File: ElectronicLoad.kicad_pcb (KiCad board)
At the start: 4 copper layers, 100 x 65 mm, 93 parts, among them J1 USB_B, J2 TagConnect, J3 ICSP, J4 Load, Q1 MTP3055VL, Q2 DMG2302U, SW1 RESET, SW2 BOOTLOADER, SW3 Control, U1 TLC272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

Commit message: Move connectors
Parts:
- moved LCD1 86.4 mm to (119.9, 102.1)
- moved C23 74.5 mm to (122.9, 94.5)
- moved C19 74.5 mm to (120.9, 94.5)
- moved C21 74.5 mm to (118.9, 94.5)
- moved RN2 74.5 mm to (120.6, 89.9)
- moved SW3 74.5 mm to (112.8, 85.3)
- moved C11 73.5 mm to (190.5, 95.0)
- moved C14 73.5 mm to (160.8, 87.9)
- moved C17 73.5 mm to (140.7, 112.0)
- moved C5 73.5 mm to (140.7, 116.6)
- moved C6 73.5 mm to (140.7, 114.3)
- moved H2 73.5 mm to (200.4, 71.7)
- moved H3 73.5 mm to (200.4, 126.7)
- moved Q1 73.5 mm to (196.6, 96.5)
- moved RN3 73.5 mm to (155.4, 114.3)
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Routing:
- net ROT_SW: track 68.0 -> 56.7 mm
- net Net-(RN1-Pad3): track 65.7 -> 55.6 mm
- net SCL: track 128.8 -> 137.0 mm
- net SDA: track 127.3 -> 134.8 mm, vias 5 -> 6
- net VLOAD: track 133.5 -> 138.9 mm
- net /D_USB-: track 20.1 -> 22.9 mm
- net /D_USB+: track 25.5 -> 28.2 mm
- net ROT_A: track 35.2 -> 36.3 mm
- net VREF2048: track 28.4 -> 27.3 mm
- net /ILOAD+: track 101.1 -> 102.1 mm
- net FAN_PWM: track 62.9 -> 62.2 mm
- net VCC: track 121.5 -> 120.9 mm
- net /XTAL2: track 17.8 -> 18.4 mm

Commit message: Cleanup
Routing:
- net ~RXLED: track 66.5 -> 36.7 mm, vias 2 -> 0
- net ~TXLED: track 46.3 -> 39.2 mm
- net SDA: track 134.8 -> 137.5 mm, vias 6 -> 5
- net Net-(RN1-Pad3): track 55.6 -> 53.7 mm
- net ROT_SW: track 56.7 -> 55.2 mm
- net SCL: track 137.0 -> 135.5 mm
- net Net-(LED3-Pad2): track 23.3 -> 21.9 mm
- net Net-(LED2-Pad2): track 24.9 -> 23.6 mm
- net /Vin-: track 11.6 -> 12.7 mm
- net Net-(LED1-Pad2): track 26.5 -> 25.5 mm
- net /XTAL2: track 18.4 -> 18.9 mm

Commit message: Cleanup
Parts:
- moved RN3 16.3 mm to (143.8, 125.7), turned to 90 degrees
- moved C2 1.61 mm to (158.0, 97.0), turned to 180 degrees
- moved C4 1.61 mm to (158.0, 99.6), turned to 180 degrees
- moved U5 1.44 mm to (158.0, 93.5), turned to 90 degrees
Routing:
- net FAN_PWM: track 62.2 -> 39.9 mm
- net Net-(LED3-Pad2): track 21.9 -> 6.94 mm
- net Net-(LED2-Pad2): track 23.6 -> 10.7 mm
- net Net-(LED1-Pad2): track 25.5 -> 15.6 mm
- net /ISET: track 19.5 -> 14.5 mm
- net SCL: track 135.5 -> 139.5 mm, vias 4 -> 5
- net Net-(RN1-Pad3): track 53.7 -> 50.3 mm
- net SDA: track 137.5 -> 140.6 mm, vias 5 -> 6
- net ~OT_SHUTDOWN: track 61.3 -> 64.0 mm
- net /~HWB: track 41.2 -> 38.6 mm
- net VREF2048: track 27.3 -> 25.4 mm
- net /ILOAD+: track 102.1 -> 100.5 mm
- net ROT_SW: track 55.2 -> 53.7 mm
- net ~RXLED: track 36.7 -> 35.6 mm
- net GND: track 298.2 -> 299.1 mm, vias 82 -> 83
- added copper zone on F.Cu, net /ILOAD+
- added copper zone on In2.Cu, net GND
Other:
- rule via_min_size: 0.6 -> 0.8

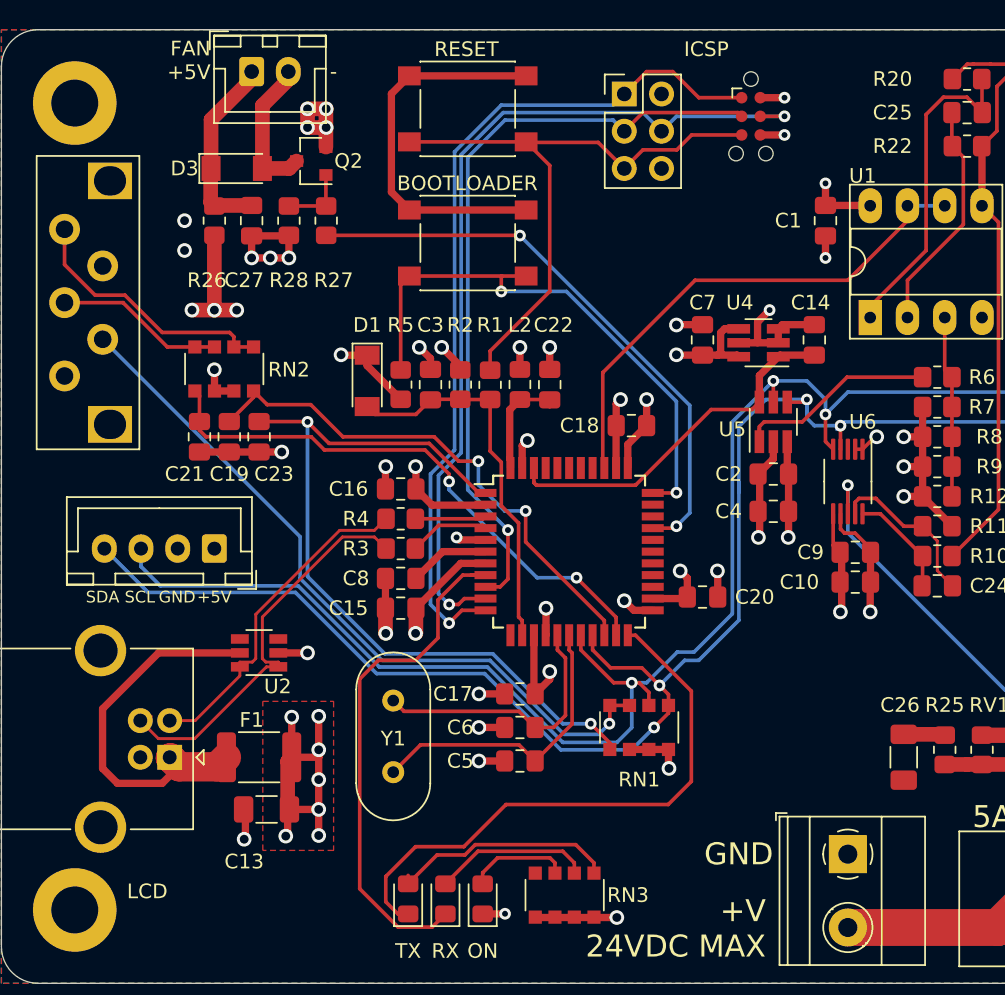
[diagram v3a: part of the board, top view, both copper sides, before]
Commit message: Tweak rotary switch footprint
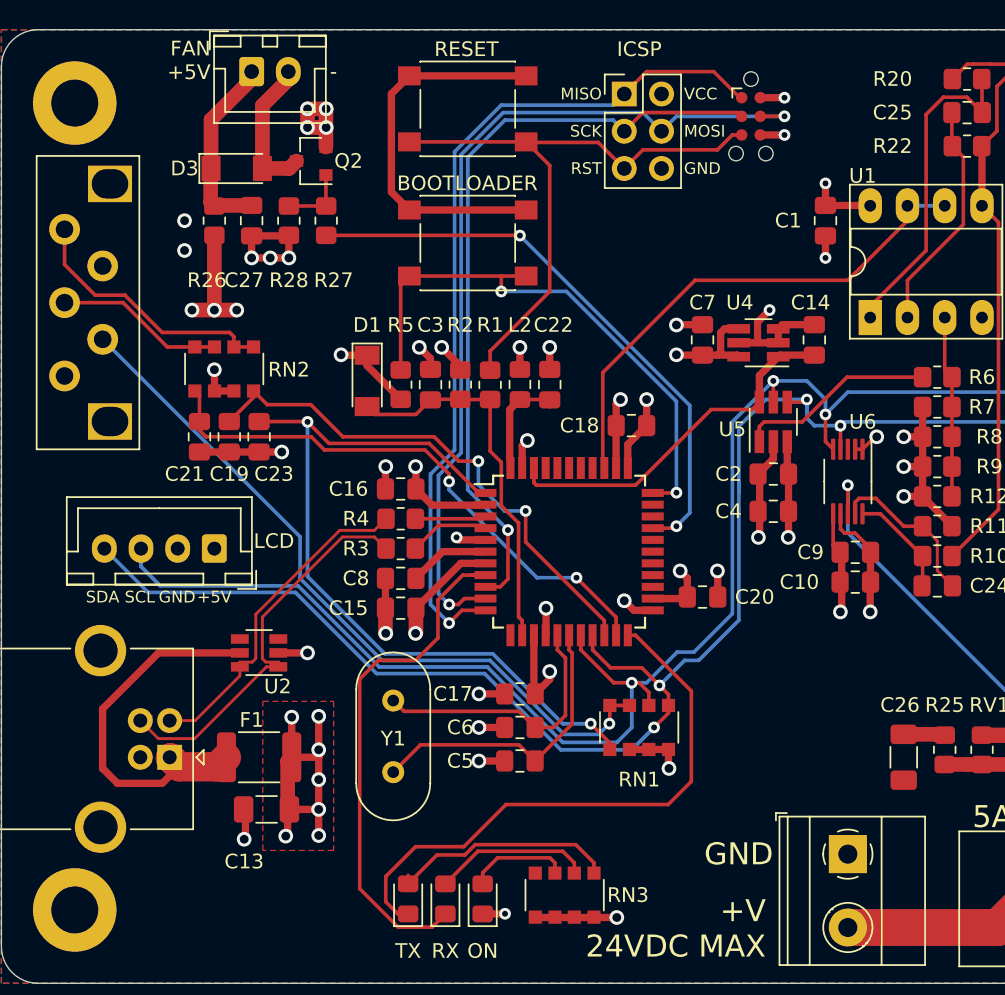
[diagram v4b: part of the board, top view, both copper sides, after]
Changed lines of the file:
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@@
       (effects (font (size 1 1) (thickness 0.15)))
     )
+    (fp_text user %R (at 5 -11) (layer F.Fab)
+      (effects (font (size 1 1) (thickness 0.15)))
+    )
     (fp_line (start -2 10) (end -2 -10) (layer F.Fab) (width 0.12))
     (fp_line (start 5 10) (end -2 10) (layer F.Fab) (width 0.12))
@@
     (fp_line (start -3.2 -10) (end -3.2 10) (layer F.CrtYd) (width 0.05))
     (fp_line (start -3.2 -10) (end 7.5 -10) (layer F.CrtYd) (width 0.05))
-    (fp_text user %R (at 5 -11) (layer F.Fab)
-      (effects (font (size 1 1) (thickness 0.15)))
-    )
     (pad A thru_hole circle (at 3.1 5 180) (size 2.1 2.1) (drill 1.2) (layers *.Cu *.Mask)
       (net 48 "Net-(RN2-Pad1)"))
@@
     (pad B thru_hole circle (at 3.1 0 180) (size 2.1 2.1) (drill 1.2) (layers *.Cu *.Mask)
       (net 47 "Net-(RN2-Pad3)"))
-    (pad MP thru_hole rect (at 0 -8.3 180) (size 3 2.5) (drill oval 2.2 2) (layers *.Cu *.Mask))
-    (pad MP thru_hole rect (at 0 8.3 180) (size 3 2.5) (drill oval 2.2 2) (layers *.Cu *.Mask))
+    (pad MP thru_hole rect (at 0 -8.1 180) (size 3 2.5) (drill oval 2.5 2) (layers *.Cu *.Mask))
+    (pad MP thru_hole rect (at 0 8.1 180) (size 3 2.5) (drill oval 2.5 2) (layers *.Cu *.Mask))
     (pad S1 thru_hole circle (at 0.5 2.5 180) (size 2.1 2.1) (drill 1.2) (layers *.Cu *.Mask)
       (net 1 GND))
@@
       (effects (font (size 0.8 0.8) (thickness 0.12)))
     )
-    (pad 2 smd roundrect (at 1.5625 0 270) (size 1.325 1.8) (layers F.Cu F.Paste F.Mask) (roundrect_rratio 0.1886777358490566)
+    (pad 2 smd roundrect (at 1.5625 0 270) (size 1.325 1.8) (layers F.Cu F.Paste F.Mask) (roundrect_rratio 0.1886769811320755)
       (net 1 GND))
-    (pad 1 smd roundrect (at -1.5625 0 270) (size 1.325 1.8) (layers F.Cu F.Paste F.Mask) (roundrect_rratio 0.1886777358490566)
+    (pad 1 smd roundrect (at -1.5625 0 270) (size 1.325 1.8) (layers F.Cu F.Paste F.Mask) (roundrect_rratio 0.1886769811320755)
       (net 62 "Net-(C26-Pad1)"))
     (model ${KISYS3DMOD}/Capacitor_SMD.3dshapes/C_1206_3216Metric.wrl
@@
       (effects (font (size 0.8 0.8) (thickness 0.12)))
     )
-    (pad 2 smd roundrect (at 1.5625 0 180) (size 1.325 1.8) (layers F.Cu F.Paste F.Mask) (roundrect_rratio 0.1886777358490566)
+    (pad 2 smd roundrect (at 1.5625 0 180) (size 1.325 1.8) (layers F.Cu F.Paste F.Mask) (roundrect_rratio 0.1886769811320755)
       (net 1 GND))
-    (pad 1 smd roundrect (at -1.5625 0 180) (size 1.325 1.8) (layers F.Cu F.Paste F.Mask) (roundrect_rratio 0.1886777358490566)
+    (pad 1 smd roundrect (at -1.5625 0 180) (size 1.325 1.8) (layers F.Cu F.Paste F.Mask) (roundrect_rratio 0.1886769811320755)
       (net 2 VCC))
     (model ${KISYS3DMOD}/Capacitor_SMD.3dshapes/C_1206_3216Metric.wrl
@@
     (effects (font (size 1 1) (thickness 0.15)) (justify left mirror))
   )
-  (gr_text GND (at 151.892 76.2) (layer B.SilkS)
-    (effects (font (size 0.8 0.8) (thickness 0.15)) (justify right mirror))
+  (gr_text GND (at 151.892 76.2) (layer F.SilkS)
+    (effects (font (size 0.8 0.8) (thickness 0.15)) (justify left))
   )
-  (gr_text RST (at 146.304 76.2) (layer B.SilkS)
-    (effects (font (size 0.8 0.8) (thickness 0.15)) (justify left mirror))
+  (gr_text RST (at 146.304 76.2) (layer F.SilkS)
+    (effects (font (size 0.8 0.8) (thickness 0.15)) (justify right))
   )
-  (gr_text MOSI (at 151.892 73.66) (layer B.SilkS)
-    (effects (font (size 0.8 0.8) (thickness 0.15)) (justify right mirror))
+  (gr_text MOSI (at 151.892 73.66) (layer F.SilkS)
+    (effects (font (size 0.8 0.8) (thickness 0.15)) (justify left))
   )
-  (gr_text SCK (at 146.304 73.66) (layer B.SilkS)
-    (effects (font (size 0.8 0.8) (thickness 0.15)) (justify left mirror))
+  (gr_text SCK (at 146.304 73.66) (layer F.SilkS)
+    (effects (font (size 0.8 0.8) (thickness 0.15)) (justify right))
   )
-  (gr_text VCC (at 151.892 71.12) (layer B.SilkS)
-    (effects (font (size 0.8 0.8) (thickness 0.15)) (justify right mirror))
+  (gr_text VCC (at 151.892 71.12) (layer F.SilkS)
+    (effects (font (size 0.8 0.8) (thickness 0.15)) (justify left))
   )
-  (gr_text MISO (at 146.304 71.12) (layer B.SilkS)
-    (effects (font (size 0.8 0.8) (thickness 0.15)) (justify left mirror))
+  (gr_text MISO (at 146.304 71.12) (layer F.SilkS)
+    (effects (font (size 0.8 0.8) (thickness 0.15)) (justify right))
   )
   (gr_text BOOTLOADER (at 132.334 77.216) (layer F.SilkS)
@@
     (effects (font (size 1 1) (thickness 0.15)) (justify left))
   )
-  (gr_text ICSP (at 151.892 68.072) (layer F.SilkS)
+  (gr_text ICSP (at 147.32 68.072) (layer F.SilkS)
     (effects (font (size 1 1) (thickness 0.15)) (justify left))
   )
@@
     (effects (font (size 0.8 0.8) (thickness 0.12)))
   )
-  (gr_text LCD (at 115.316 125.476) (layer F.SilkS)
+  (gr_text LCD (at 123.952 101.6) (layer F.SilkS)
     (effects (font (size 1 1) (thickness 0.15)))
   )
@@
   (segment (start 134.62 105.918) (end 134.62 97.028) (width 0.25) (layer B.Cu) (net 12))
   (segment (start 135.89 107.188) (end 134.62 105.918) (width 0.25) (layer B.Cu) (net 12))
-  (segment (start 151.13 69.596) (end 149.352 69.596) (width 0.25) (layer F.Cu) (net 12))
-  (segment (start 152.908 71.374) (end 151.13 69.596) (width 0.25) (layer F.Cu) (net 12))
-  (segment (start 149.352 69.596) (end 147.828 71.12) (width 0.25) (layer F.Cu) (net 12) (status 20))
-  (segment (start 155.829 71.374) (end 152.908 71.374) (width 0.25) (layer F.Cu) (net 12) (status 10))
+  (segment (start 149.352 69.596) (end 147.828 71.12) (width 0.25) (layer F.Cu) (net 12))
+  (segment (start 153.924 69.596) (end 149.352 69.596) (width 0.25) (layer F.Cu) (net 12))
+  (segment (start 155.702 71.374) (end 153.924 69.596) (width 0.25) (layer F.Cu) (net 12))
+  (segment (start 155.829 71.374) (end 155.702 71.374) (width 0.25) (layer F.Cu) (net 12))
   (segment (start 116.890001 116.382001) (end 116.890001 116.36201) (width 2) (layer F.Cu) (net 13) (status 30))
   (segment (start 117.49 116.982) (end 116.890001 116.382001) (width 2) (layer F.Cu) (net 13) (status 30))
@@
   (segment (start 141.176 74.422) (end 146.05 74.422) (width 0.25) (layer F.Cu) (net 27) (status 10))
   (segment (start 141.14 74.386) (end 141.176 74.422) (width 0.25) (layer F.Cu) (net 27) (status 30))
-  (segment (start 152.419556 73.914) (end 155.829 73.914) (width 0.25) (layer F.Cu) (net 27) (status 20))
-  (segment (start 151.403556 74.93) (end 152.419556 73.914) (width 0.25) (layer F.Cu) (net 27))
-  (segment (start 149.098 74.93) (end 151.403556 74.93) (width 0.25) (layer F.Cu) (net 27))
-  (segment (start 147.828 76.2) (end 149.098 74.93) (width 0.25) (layer F.Cu) (net 27) (status 10))
+  (segment (start 155.194 73.914) (end 155.829 73.914) (width 0.25) (layer F.Cu) (net 27))
+  (segment (start 154.178 74.93) (end 155.194 73.914) (width 0.25) (layer F.Cu) (net 27))
+  (segment (start 149.098 74.93) (end 154.178 74.93) (width 0.25) (layer F.Cu) (net 27))
+  (segment (start 147.828 76.2) (end 149.098 74.93) (width 0.25) (layer F.Cu) (net 27))
   (segment (start 133.6255 104.14) (end 135.4495 102.316) (width 0.5) (layer F.Cu) (net 28) (status 10))
   (segment (start 138.37 102.316) (end 135.4495 102.316) (width 0.5) (layer F.Cu) (net 28) (status 10))
